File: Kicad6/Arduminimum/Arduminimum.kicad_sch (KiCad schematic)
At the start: 16 parts, among them J1 Jack-DC, J2 Conn_01x02_Female, J3 Conn_01x02_Female, J4 Conn_01x02_Female, SW1 SW_SPDT, U1 LM7805

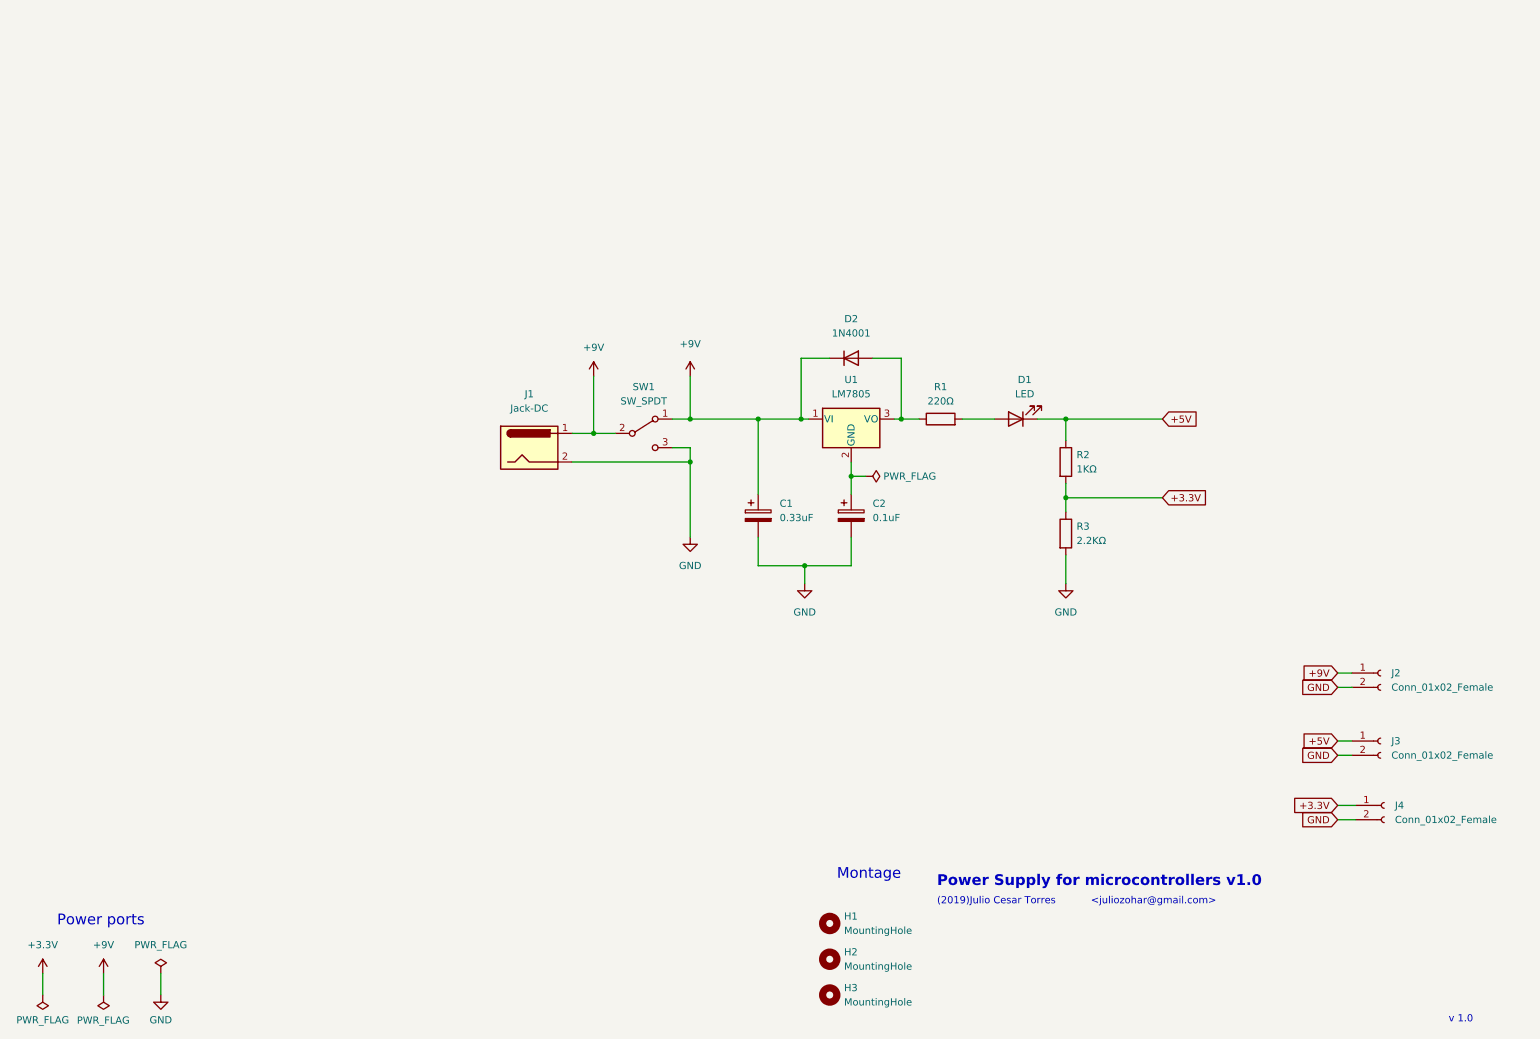
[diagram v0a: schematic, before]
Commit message: [func] inclui microcontroladora no schematic
Signed-off-by: Julio Cesar Torres <julio.cesartorres@mcn.gouv.qc.ca>
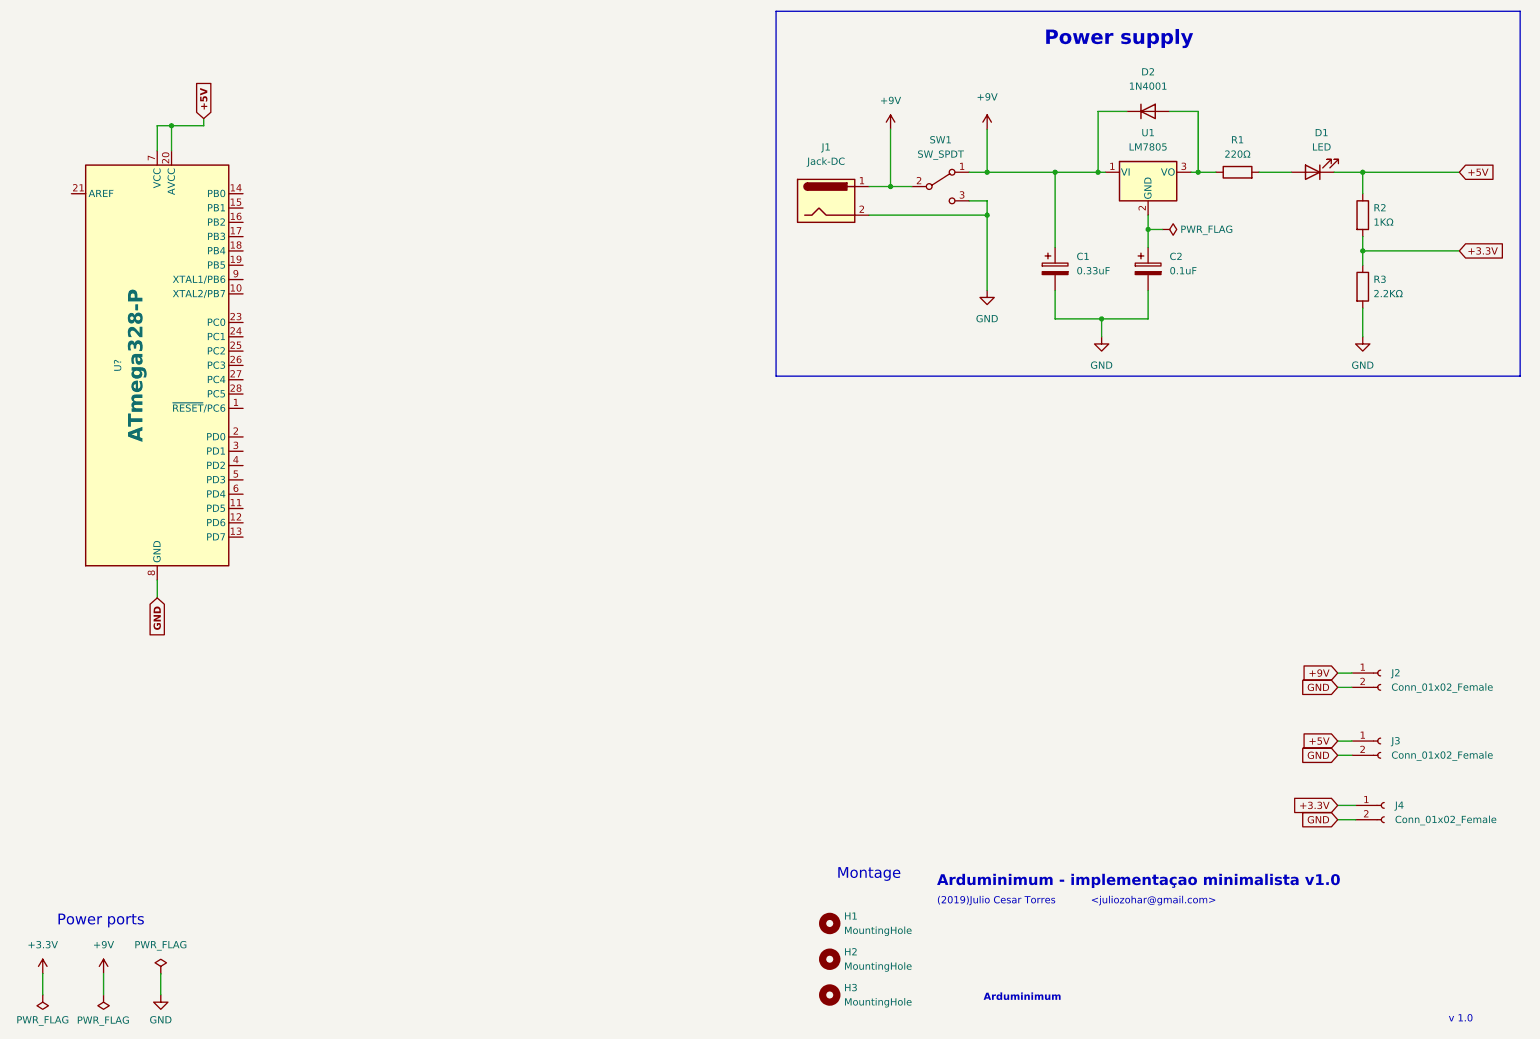
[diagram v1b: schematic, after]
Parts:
- added U?: ATmega328-P, Package_DIP:DIP-28_W7.62mm, symbol MCU_Microchip_ATmega:ATmega328-P
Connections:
- net +5V: now also U?.20 (AVCC), U?.7 (VCC)
- net GND: now also U?.22 (GND), U?.8 (GND)
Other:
- note added: "Arduminimum"
- note added: "Arduminimum - implementaçao minimalista v1.0"
- note added: "Power supply"
- note removed: "Power Supply for microcontrollers v1.0"
- moved on the sheet: C1, C2, D1, D2, J1, R1, R2, R3, SW1, U1

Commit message: [func] melhorias do circuito; inclusao de novas partes
Signed-off-by: Julio Cesar Torres <julio.cesartorres@mcn.gouv.qc.ca>
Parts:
- added BZ1: Buzzer, symbol Device:Buzzer
- added C3, C4: 22pF, symbol Device:C
- added D3: LED, symbol Device:LED
- added D4: LED_RGBK, LED_THT:LED_D5.0mm-4_RGB, symbol Device:LED_RGBK
- added J5: Pins analogiques, Connector_PinSocket_2.54mm:PinSocket_1x06_P2.54mm_Vertical, symbol Connector:Conn_01x06_Male
- added R4, R6: R, symbol Device:R
- added R5: 470Ω, symbol Device:R
- added R7, R8, R9: 220Ω, symbol Device:R
- added Y1: Crystal, symbol Device:Crystal
- gave numbers to parts that had none: 1
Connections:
- net +5V: now also R5.2
- net GND: now also BZ1.2 (+), C3.2, C4.2, D3.1 (K), D4.4 (K)
- net at U2.1 (~{RESET}/PC6): now also R5.1
- net at U2.10 (XTAL2/PB7): now also C4.1, Y1.1
- net at U2.11 (PD5): now also R6.1
- net at U2.13 (PD7): now also R4.1
- net A0: now reaches U2.23 (PC0)
- net A0: now also J5.1 (Pin_1)
- net A1: now reaches U2.24 (PC1)
- net A1: now also J5.2 (Pin_2)
- net A2: now reaches U2.25 (PC2)
- net A2: now also J5.3 (Pin_3)
- net A3: now reaches U2.26 (PC3)
- net A3: now also J5.4 (Pin_4)
- net A4: now reaches U2.27 (PC4)
- net A4: now also J5.5 (Pin_5)
- net A5: now reaches U2.28 (PC5)
- net A5: now also J5.6 (Pin_6)
- net at U2.9 (XTAL1/PB6): now also C3.1, Y1.2
- new net: BZ1.1 (-), R6.2
- new net: D4.2 (GA), R8.1
- new net: D3.2 (A), R4.2
- new net: D4.3 (BA), R9.1
- new net: D4.1 (RA), R7.1
- new net D6: R7.2
- new net D7: R8.2
- new net D8: R9.2
- no-connect marks 0 -> 1
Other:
- note added: "<juliozohar@gmail.com> @torjc01"
- note removed: "<juliozohar@gmail.com>"
- moved on the sheet: J2, J3, J4, U2

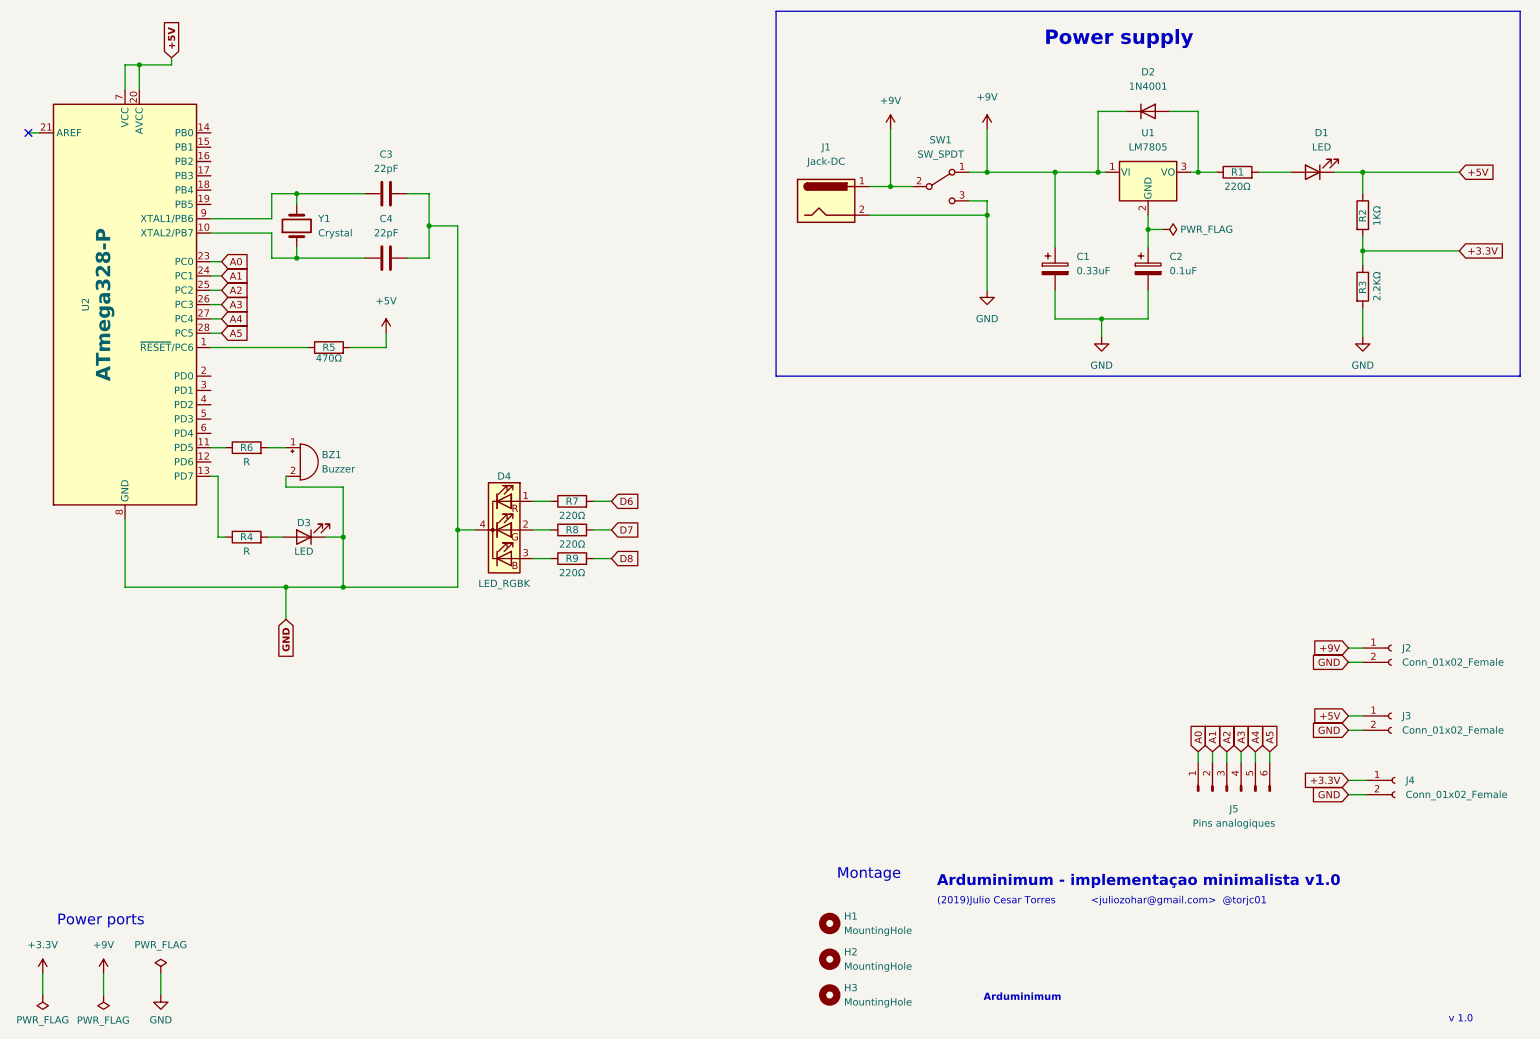
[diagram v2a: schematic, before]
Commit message: [func] adiciona novos componentes ao circuito; documenta
Signed-off-by: Julio Cesar Torres <julio.cesartorres@mcn.gouv.qc.ca>
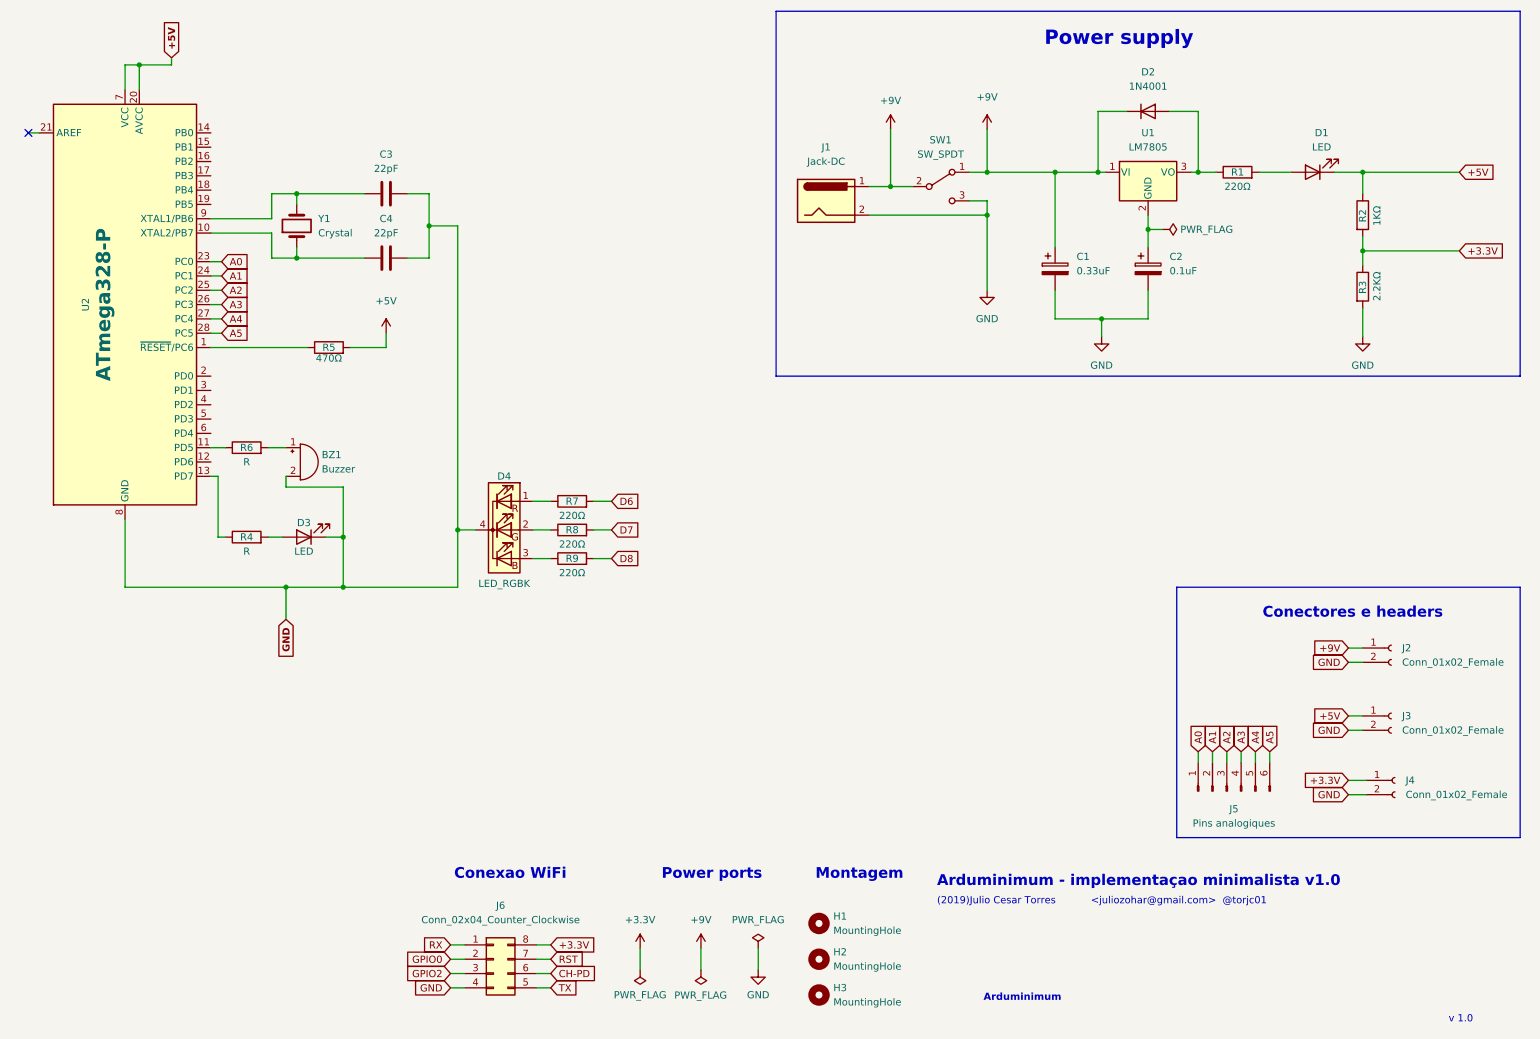
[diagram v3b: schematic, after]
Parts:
- added J6: Conn_02x04_Counter_Clockwise, symbol Connector_Generic:Conn_02x04_Counter_Clockwise
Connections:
- net +3.3V: now also J6.8 (Pin_8)
- net GND: now also J6.4 (Pin_4)
- new net CH-PD: J6.6 (Pin_6)
- new net GPIO0: J6.2 (Pin_2)
- new net GPIO2: J6.3 (Pin_3)
- new net RST: J6.7 (Pin_7)
- new net RX: J6.1 (Pin_1)
- new net TX: J6.5 (Pin_5)
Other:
- note added: "Conectores e headers"
- note added: "Conexao WiFi"
- note added: "Montagem"
- note removed: "Montage"
- moved on the sheet: H1, H2, H3

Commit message: [func] evolui o documento de schema
Signed-off-by: Julio Cesar Torres <julio.cesartorres@mcn.gouv.qc.ca>
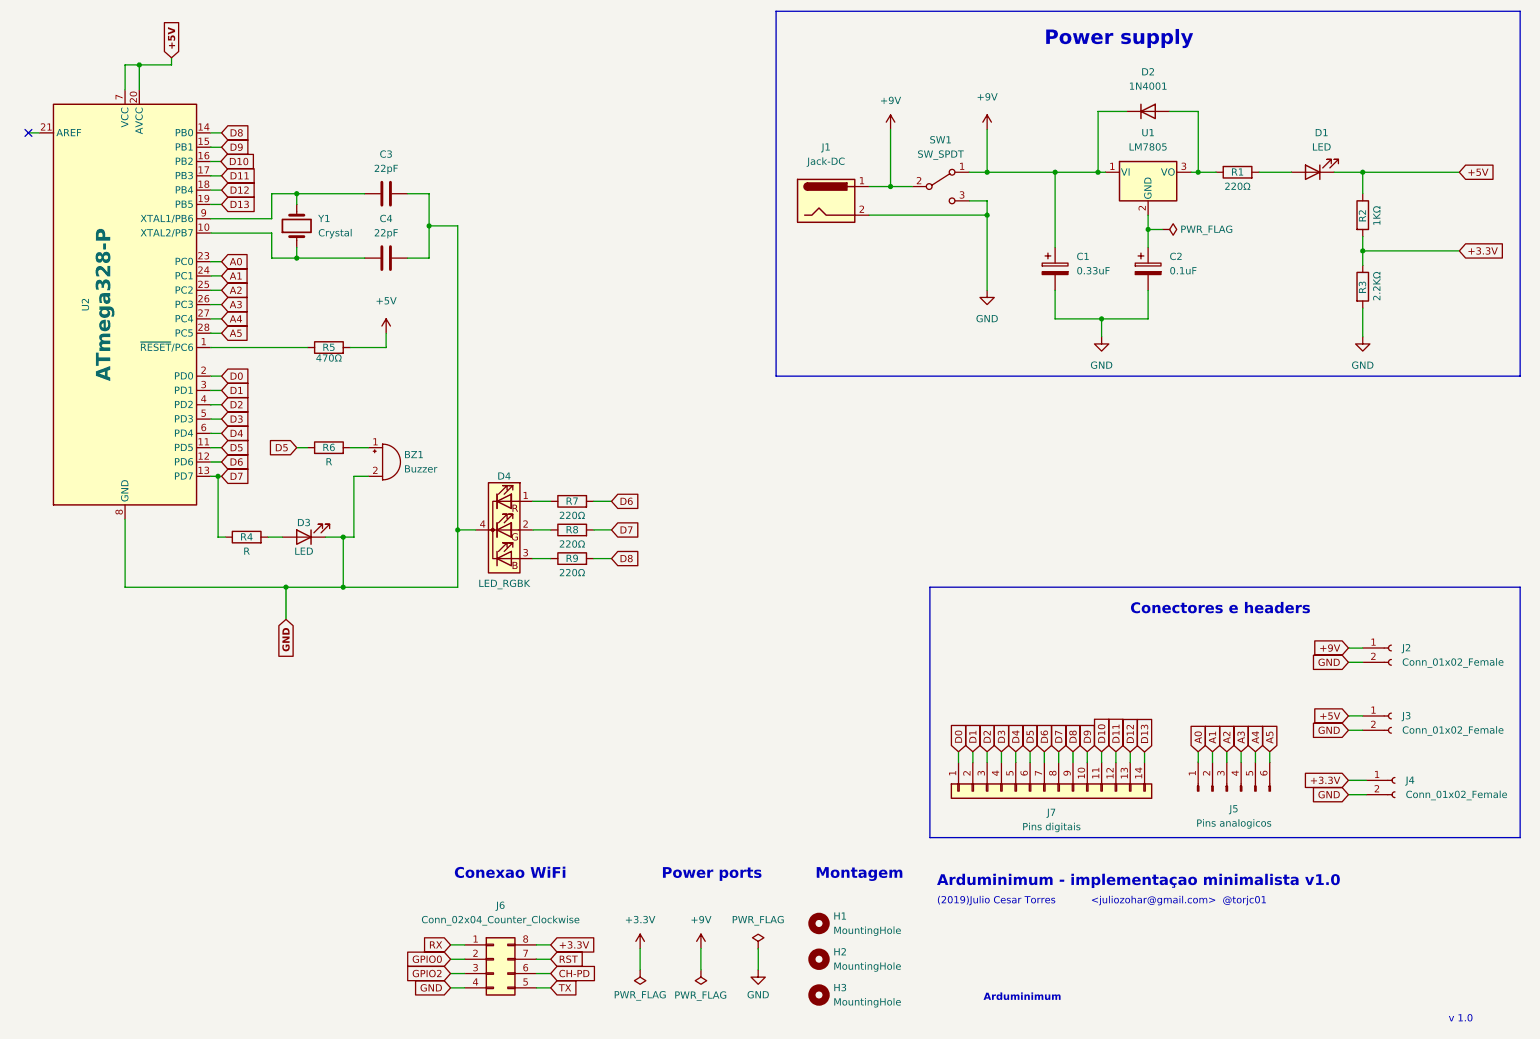
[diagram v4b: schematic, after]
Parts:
- added J7: Pins digitais, Connector_PinSocket_2.54mm:PinSocket_1x14_P2.54mm_Vertical, symbol Connector_Generic:Conn_01x14
- J5: value Pins analogiques -> Pins analogicos
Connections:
- net D6: now also U2.12 (PD6), J7.7 (Pin_7)
- net D7: now also R4.1, U2.13 (PD7), J7.8 (Pin_8)
- net D8: now also U2.14 (PB0), J7.9 (Pin_9)
- net D5: now reaches R6.1, U2.11 (PD5)
- net D5: now also J7.6 (Pin_6)
- net D9: now reaches U2.15 (PB1)
- net D9: now also J7.10 (Pin_10)
- net D10: now reaches U2.16 (PB2)
- net D10: now also J7.11 (Pin_11)
- net D11: now reaches U2.17 (PB3)
- net D11: now also J7.12 (Pin_12)
- net D12: now reaches U2.18 (PB4)
- net D12: now also J7.13 (Pin_13)
- net D13: now reaches U2.19 (PB5)
- net D13: now also J7.14 (Pin_14)
- net D0: now reaches U2.2 (PD0)
- net D0: now also J7.1 (Pin_1)
- net D1: now reaches U2.3 (PD1)
- net D1: now also J7.2 (Pin_2)
- net D2: now reaches U2.4 (PD2)
- net D2: now also J7.3 (Pin_3)
- net D3: now reaches U2.5 (PD3)
- net D3: now also J7.4 (Pin_4)
- net D4: now reaches U2.6 (PD4)
- net D4: now also J7.5 (Pin_5)
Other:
- moved on the sheet: BZ1, R6
